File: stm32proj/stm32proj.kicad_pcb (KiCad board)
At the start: 2 copper layers, 24.1 x 21.6 mm, 29 parts, among them J1 Conn_01x04_Pin, J2 Conn_01x04_Pin, J3 USB_C_Receptacle_USB2.0_14P, U1 STM32F103C8Tx, U2 AMS1117-3.3, U3 AS5600, Y1 8MHz

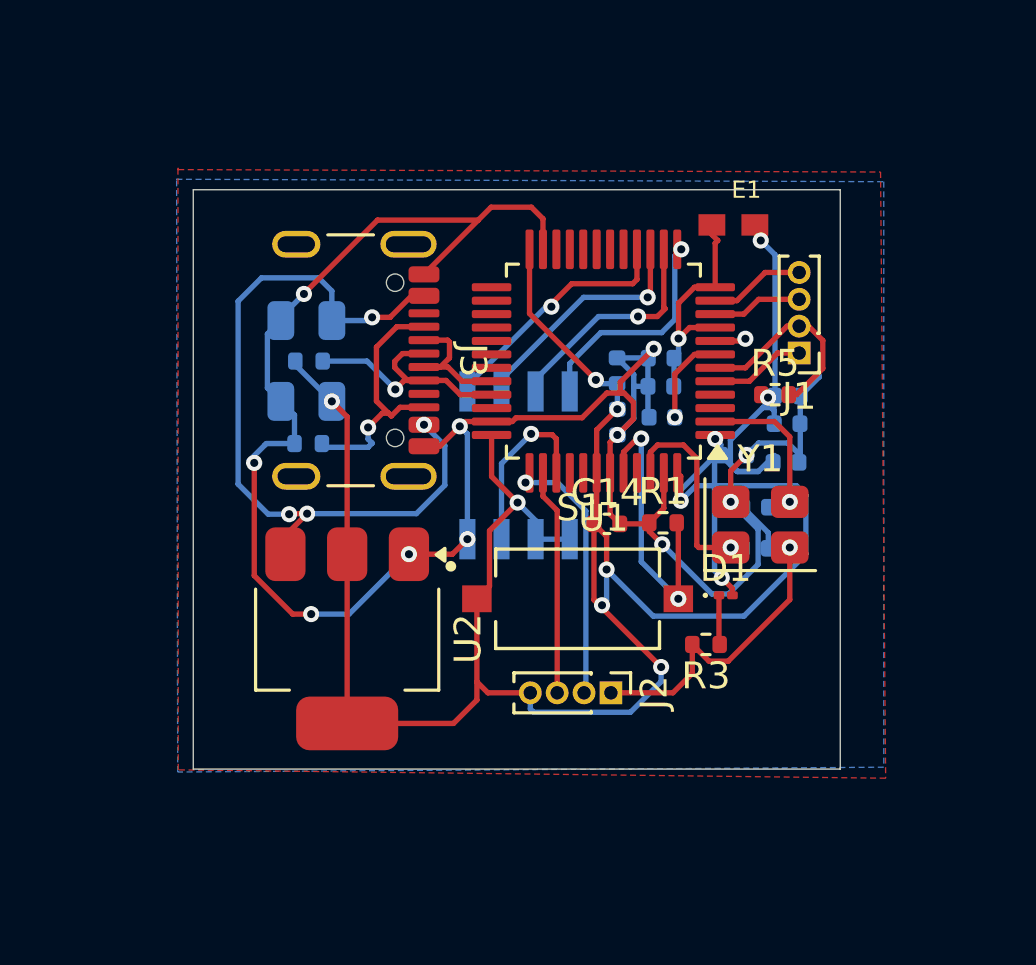
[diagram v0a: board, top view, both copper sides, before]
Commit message: added mounting holes
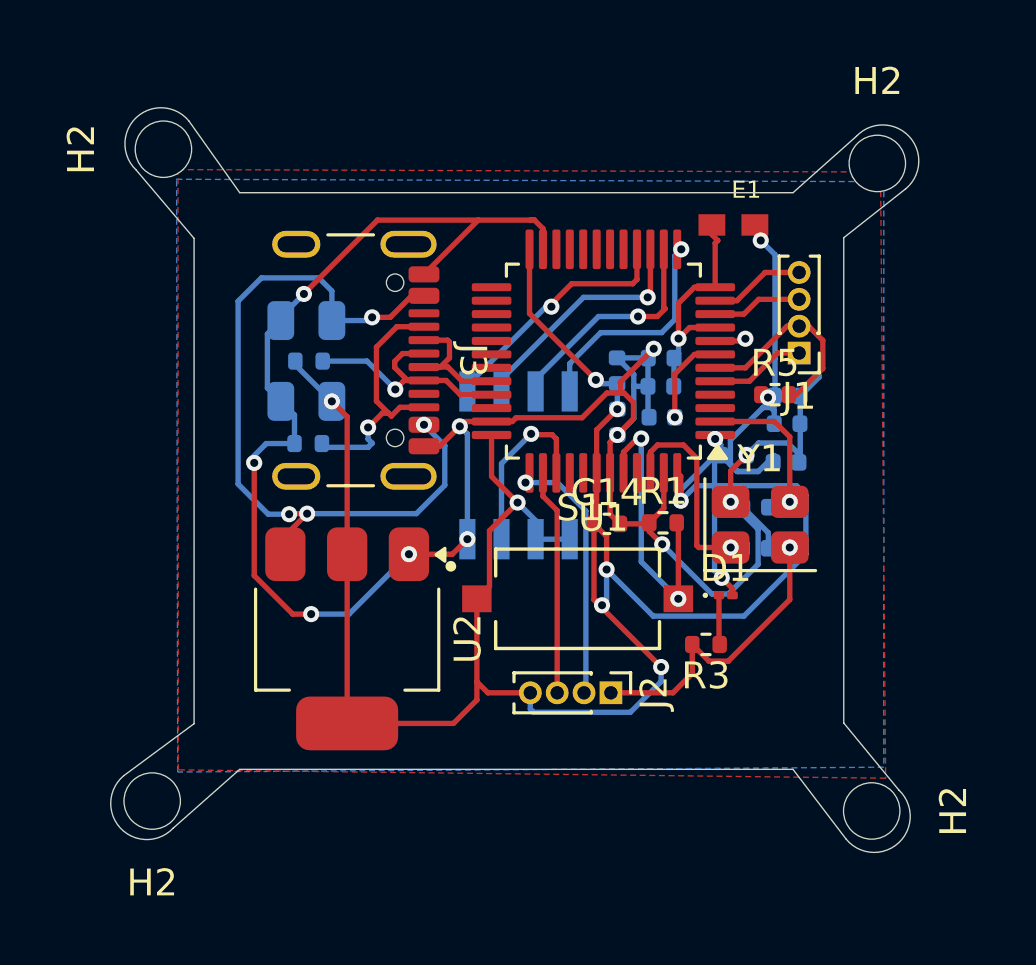
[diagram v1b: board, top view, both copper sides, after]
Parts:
- added H2: MountingHole, MountingHole:MountingHole_2.1mm, F.Cu at (137.6, 81.4)
- added H2: MountingHole, MountingHole:MountingHole_2.1mm, F.Cu at (110.8, 81.1)
- added H2: MountingHole, MountingHole:MountingHole_2.1mm, F.Cu at (111.2, 56.8)
- added H2: MountingHole, MountingHole:MountingHole_2.1mm, F.Cu at (137.8, 57.3)
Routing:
- net GND: track 100.1 -> 99.5 mm
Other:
- board size 24.1 x 21.6 mm -> 30.1 x 27.7 mm
